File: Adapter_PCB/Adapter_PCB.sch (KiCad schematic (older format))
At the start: 3 parts, among them J1 Conn_01x10, J2 USB_B_Micro, J3 Conn_01x06

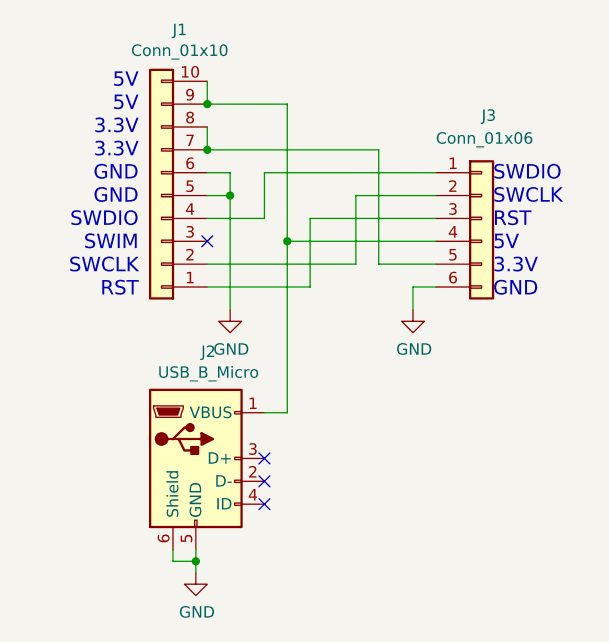
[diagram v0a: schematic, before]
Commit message: Add 4 pin connector, change connector pinout, add silkscreen
Only one of reducing connectors can be populated.
In silkscreen are now connector pinouts diagrams and logo with QR code.
Connector pinout was rearranged to mach IDC cable with lock on different sides.
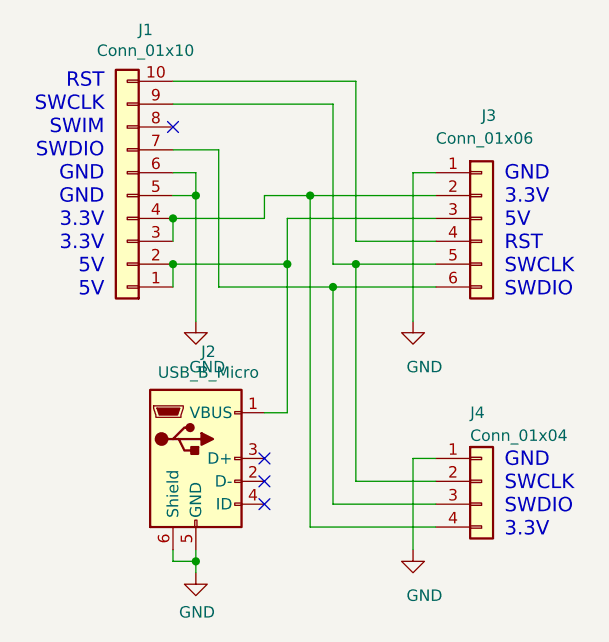
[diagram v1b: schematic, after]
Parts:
- added J4: Conn_01x04, Connector_PinHeader_2.54mm:PinHeader_1x04_P2.54mm_Horizontal, symbol Connector_Generic:Conn_01x04
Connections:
- net GND: now also J3.1 (Pin_1), J4.1 (Pin_1); no longer J3.6 (Pin_6)
- net at J1.1 (Pin_1), J3.3 (Pin_3): now also J1.2 (Pin_2), J2.1 (VBUS)
- net at J1.10 (Pin_10), J3.4 (Pin_4): no longer J1.9 (Pin_9), J2.1 (VBUS)
- net at J3.2 (Pin_2): now also J1.3 (Pin_3), J1.4 (Pin_4), J4.4 (Pin_4); no longer J1.2 (Pin_2)
- new net: J1.9 (Pin_9), J3.5 (Pin_5), J4.2 (Pin_2)
- new net: J1.7 (Pin_7), J3.6 (Pin_6), J4.3 (Pin_3)
- now unconnected: J1.8 (Pin_8)
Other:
- note added: "GND\nSWCLK\nSWDIO\n3.3V"
- note added: "RST\nSWCLK\nSWIM\nSWDIO\nGND\nGND\n3.3V\n3.3V\n5V\n5V"
- note added: "\n\n\n\n\nGND\n3.3V\n5V\nRST\nSWCLK\nSWDIO"
- note removed: "5V\n5V\n3.3V\n3.3V\nGND\nGND\nSWDIO\nSWIM\nSWCLK\nRST"
- note removed: "SWDIO\nSWCLK\nRST\n5V\n3.3V\nGND"
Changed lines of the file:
@@
 EESchema Schematic File Version 4
+LIBS:Adapter_PCB-cache
 EELAYER 26 0
 EELAYER END
@@
 $EndDescr
 $Comp
-L Connector_Generic:Conn_01x10 J1
-U 1 1 5C5D86D7
-P 3600 3350
-F 0 "J1" H 3520 2625 50  0000 C CNN
-F 1 "Conn_01x10" H 3520 2716 50  0000 C CNN
-F 2 "Connector_IDC:IDC-Header_2x05_P2.54mm_Horizontal" H 3600 3350 50  0001 C CNN
-F 3 "~" H 3600 3350 50  0001 C CNN
-	1    3600 3350
-	-1   0    0    1
-$EndComp
-$Comp
 L Connector_Generic:Conn_01x06 J3
 U 1 1 5C5D886D
@@
 	1    0    0    -1
 $EndComp
-Text Notes 3500 3800 2    63   ~ 0
-5V\n5V\n3.3V\n3.3V\nGND\nGND\nSWDIO\nSWIM\nSWCLK\nRST
-Text Notes 5050 3800 0    63   ~ 0
-SWDIO\nSWCLK\nRST\n5V\n3.3V\nGND
-Wire Wire Line
-	3800 3650 4450 3650
-Wire Wire Line
-	4450 3650 4450 3350
-Wire Wire Line
-	4450 3350 4800 3350
-Wire Wire Line
-	4800 3650 4550 3650
-Wire Wire Line
-	4550 3650 4550 3150
-Wire Wire Line
-	4550 3150 3800 3150
-Wire Wire Line
-	3800 3050 3800 3150
-Connection ~ 3800 3150
-Wire Wire Line
-	4800 3250 4050 3250
-Wire Wire Line
-	4050 3250 4050 3450
-Wire Wire Line
-	4050 3450 3800 3450
-Wire Wire Line
-	4800 3550 4150 3550
-Wire Wire Line
-	4150 3550 4150 2950
-Wire Wire Line
-	4150 2950 3800 2950
-Wire Wire Line
-	3800 2850 3800 2950
-Connection ~ 3800 2950
-Wire Wire Line
-	4800 3450 4250 3450
-Wire Wire Line
-	4250 3450 4250 3750
-Wire Wire Line
-	4250 3750 3800 3750
-NoConn ~ 3800 3550
+Text Notes 5100 3800 0    63   ~ 0
+\n\n\n\n\nGND\n3.3V\n5V\nRST\nSWCLK\nSWDIO
 $Comp
 L Connector:USB_B_Micro J2
@@
 NoConn ~ 4050 4500
 Wire Wire Line
-	4150 3550 4150 4300
-Wire Wire Line
 	4150 4300 4050 4300
-Connection ~ 4150 3550
-Wire Wire Line
-	3800 3250 3900 3250
-Wire Wire Line
-	3900 3250 3900 3350
-Wire Wire Line
-	3800 3350 3900 3350
-Connection ~ 3900 3350
-Wire Wire Line
-	3900 3350 3900 3850
-Wire Wire Line
-	4800 3750 4700 3750
-Wire Wire Line
-	4700 3750 4700 3850
-$Comp
-L power:GND #PWR0101
-U 1 1 5C5DADF3
-P 4700 3850
-F 0 "#PWR0101" H 4700 3600 50  0001 C CNN
-F 1 "GND" H 4705 3677 50  0000 C CNN
-F 2 "" H 4700 3850 50  0001 C CNN
-F 3 "" H 4700 3850 50  0001 C CNN
-	1    4700 3850
-	1    0    0    -1
-$EndComp
-$Comp
-L power:GND #PWR0102
-U 1 1 5C5DAE0B
-P 3900 3850
-F 0 "#PWR0102" H 3900 3600 50  0001 C CNN
-F 1 "GND" H 3905 3677 50  0000 C CNN
-F 2 "" H 3900 3850 50  0001 C CNN
-F 3 "" H 3900 3850 50  0001 C CNN
-	1    3900 3850
-	1    0    0    -1
-$EndComp
 $Comp
 L power:GND #PWR0103
@@
 	3750 4950 3750 5000
 Connection ~ 3750 4950
+$Comp
+L Connector_Generic:Conn_01x04 J4
+U 1 1 5C64BED8
+P 5000 4600
+F 0 "J4" H 4950 4900 50  0000 L CNN
+F 1 "Conn_01x04" H 4950 4800 50  0000 L CNN
+F 2 "Connector_PinHeader_2.54mm:PinHeader_1x04_P2.54mm_Horizontal" H 5000 4600 50  0001 C CNN
+F 3 "~" H 5000 4600 50  0001 C CNN
+	1    5000 4600
+	1    0    0    -1
+$EndComp
+Text Notes 5100 4850 0    63   ~ 0
+GND\nSWCLK\nSWDIO\n3.3V
+Text Notes 3350 3800 2    63   ~ 0
+RST\nSWCLK\nSWIM\nSWDIO\nGND\nGND\n3.3V\n3.3V\n5V\n5V
+Wire Wire Line
+	3650 3750 3650 3650
+Wire Wire Line
+	4150 4300 4150 3650
+Wire Wire Line
+	4150 3450 4800 3450
+Wire Wire Line
+	3650 3650 4150 3650
+Connection ~ 4150 3650
+Wire Wire Line
+	4150 3650 4150 3450
+Wire Wire Line
+	3650 3450 3650 3550
+Wire Wire Line
+	3650 3450 4050 3450
+Wire Wire Line
+	4050 3450 4050 3350
+Wire Wire Line
+	4050 3350 4250 3350
+Wire Wire Line
+	4800 4800 4250 4800
+Wire Wire Line
+	4250 4800 4250 3350
+Connection ~ 4250 3350
+Wire Wire Line
+	4250 3350 4800 3350
+Wire Wire Line
+	4800 3250 4700 3250
+Wire Wire Line
+	4700 3250 4700 3900
+Wire Wire Line
+	3650 3350 3750 3350
+Wire Wire Line
+	3650 3250 3750 3250
+Wire Wire Line
+	3750 3250 3750 3350
+Connection ~ 3750 3350
+Connection ~ 3650 3450
+Connection ~ 3650 3650
+$Comp
+L Connector_Generic:Conn_01x10 J1
+U 1 1 5C64E996
+P 3450 3350
+F 0 "J1" H 3370 2625 50  0000 C CNN
+F 1 "Conn_01x10" H 3370 2716 50  0000 C CNN
+F 2 "Connector_IDC:IDC-Header_2x05_P2.54mm_Horizontal" H 3450 3350 50  0001 C CNN
+F 3 "~" H 3450 3350 50  0001 C CNN
+	1    3450 3350
+	-1   0    0    1
+$EndComp
+Wire Wire Line
+	4800 4500 4700 4500
+Wire Wire Line
+	4700 4500 4700 4900
+$Comp
+L power:GND #PWR0101
+U 1 1 5C651333
+P 4700 4900
+F 0 "#PWR0101" H 4700 4650 50  0001 C CNN
+F 1 "GND" H 4750 4700 50  0000 C CNN
+F 2 "" H 4700 4900 50  0001 C CNN
+F 3 "" H 4700 4900 50  0001 C CNN
+	1    4700 4900
+	1    0    0    -1
+$EndComp
+$Comp
+L power:GND #PWR0102
+U 1 1 5C65134D
+P 4700 3900
+F 0 "#PWR0102" H 4700 3650 50  0001 C CNN
+F 1 "GND" H 4750 3700 50  0000 C CNN
+F 2 "" H 4700 3900 50  0001 C CNN
+F 3 "" H 4700 3900 50  0001 C CNN
+	1    4700 3900
+	1    0    0    -1
+$EndComp
+$Comp
+L power:GND #PWR0104
+U 1 1 5C6513A0
+P 3750 3900
+F 0 "#PWR0104" H 3750 3650 50  0001 C CNN
+F 1 "GND" H 3800 3700 50  0000 C CNN
+F 2 "" H 3750 3900 50  0001 C CNN
+F 3 "" H 3750 3900 50  0001 C CNN
+	1    3750 3900
+	1    0    0    -1
+$EndComp
+Wire Wire Line
+	3750 3350 3750 3900
+Wire Wire Line
+	3650 3150 3850 3150
+Wire Wire Line
+	3850 3150 3850 3750
+Wire Wire Line
+	3850 3750 4350 3750
+Wire Wire Line
+	4800 3650 4450 3650
+Wire Wire Line
+	4350 3650 4350 2950
+Wire Wire Line
+	4350 2950 3650 2950
+NoConn ~ 3650 3050
+Wire Wire Line
+	4800 3550 4450 3550
+Wire Wire Line
+	4450 3550 4450 2850
+Wire Wire Line
+	4450 2850 3650 2850
+Wire Wire Line
+	4800 4700 4350 4700
+Wire Wire Line
+	4350 4700 4350 3750
+Connection ~ 4350 3750
+Wire Wire Line
+	4350 3750 4800 3750
+Wire Wire Line
+	4800 4600 4450 4600
+Wire Wire Line
+	4450 4600 4450 3650
+Connection ~ 4450 3650
+Wire Wire Line
+	4450 3650 4350 3650
 $EndSCHEMATC
